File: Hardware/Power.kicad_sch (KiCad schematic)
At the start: 0 parts

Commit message: RP3254B power connections
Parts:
- added L2: L_Small, symbol Device:L_Small
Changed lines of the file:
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@@
 		(company "J. Thweatt")
 	)
+	(symbol
+		(lib_id "Device:L_Small")
+		(at 179.07 127 0)
+		(unit 1)
+		(body_style 1)
+		(exclude_from_sim no)
+		(in_bom yes)
+		(on_board yes)
+		(in_pos_files yes)
+		(dnp no)
+		(fields_autoplaced yes)
+		(property "Reference" "L2"
+			(at 180.34 125.7299 0)
+			(show_name no)
+			(do_not_autoplace no)
+			(effects
+				(font
+					(size 1.27 1.27)
+				)
+				(justify left)
+			)
+		)
+		(property "Value" "L_Small"
+			(at 180.34 128.2699 0)
+			(show_name no)
+			(do_not_autoplace no)
+			(effects
+				(font
+					(size 1.27 1.27)
+				)
+				(justify left)
+			)
+		)
+		(property "Footprint" ""
+			(at 179.07 127 0)
+			(hide yes)
+			(show_name no)
+			(do_not_autoplace no)
+			(effects
+				(font
+					(size 1.27 1.27)
+				)
+			)
+		)
+		(property "Datasheet" ""
+			(at 179.07 127 0)
+			(hide yes)
+			(show_name no)
+			(do_not_autoplace no)
+			(effects
+				(font
+					(size 1.27 1.27)
+				)
+			)
+		)
+		(property "Description" "Inductor, small symbol"
+			(at 179.07 127 0)
+			(hide yes)
+			(show_name no)
+			(do_not_autoplace no)
+			(effects
+				(font
+					(size 1.27 1.27)
+				)
+			)
+		)
+		(pin "2"
+		)
+		(pin "1"
+		)
+		(instances
+			(project "digichiver"
+				(path "/51de4045-d2a2-42d9-b145-319acd726bb6/3f31dd03-db19-4d71-92cd-90eb39c94774"
+					(reference "L2")
+					(unit 1)
+				)
+			)
+		)
+	)
 )

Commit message: sync
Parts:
- added C31: 10uF, symbol Device:C
- added C32: 22uF, symbol Device:C
- added J2: USB_C_Receptacle, symbol Connector:USB_C_Receptacle
- added L3: 1uH, symbol Device:L_Small
- added R14: 1k, symbol Device:R_US
- added U7: TLV61046A, symbol Digichiver:TLV61046A
- added U8: TPS62903, symbol Digichiver:TPS62903
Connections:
- new net: J2.A1 (GND), J2.A12 (GND), J2.B1 (GND), J2.B12 (GND)
- new net: J2.A4 (VBUS), J2.A9 (VBUS), J2.B4 (VBUS), J2.B9 (VBUS)
- new net: L3.1, U8.2 (SW)
- no-connect marks 0 -> 2
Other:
- moved on the sheet: L2

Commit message: power
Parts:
- removed J2: USB_C_Receptacle, symbol Connector:USB_C_Receptacle
- removed L3: 1uH, symbol Device:L_Small
- added C33: 1uF, symbol Device:C
- added C34: 4.7uF, symbol Device:C
- added C35: 22uF, symbol Device:C
- added J3, J4: 61300211121, symbol Connector:Conn_01x02_Pin
- added R15: 18K, symbol Device:R_US
- added R16: 71.5k, symbol Device:R_US
- added R17: 45.3K, symbol Device:R_US
- added R18: 10K, symbol Device:R_US
- L2: value L_Small -> 15uH
- R14: value 1k -> 732k
- U8: value TPS62903 -> TPSM84338
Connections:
- net +5V: now reaches L2.1
- net +5V: now also C31.1, U7.4 (EN), U7.6 (VIN), U8.1 (EN), U8.6 (VIN), C33.1
- net at L2.2: now also U7.1 (SW)
- net +9V_RAW: now reaches R14.1
- net +9V_RAW: now also U7.5 (VOUT), C34.1, J4.1 (Pin_1)
- net at R14.2: now also U7.3 (FB), R16.1
- net GND: now reaches U7.2 (GND)
- net GND: now also C31.2, C32.2, U8.3 (GND), U8.9 (RT/SYNC), C33.2, C34.2, C35.2, R15.2, R16.2, R18.2
- net +3V3_RAW: now reaches C32.1
- net +3V3_RAW: now also U8.4 (VOUT), C35.1, J3.1 (Pin_1), R17.1
- net at U8.2 (FB): now also R17.2, R18.1
- net at U8.7 (MODE): now also R15.1
- new net +3.3V: J3.2 (Pin_2)
- new net +9V: J4.2 (Pin_2)
- no-connect marks 2 -> 1
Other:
- moved on the sheet: C31, C32, L2, R14, U7

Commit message: footprint assignment
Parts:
- C31: footprint (none) -> Capacitor_SMD:C_0402_1005Metric; MPN (none) -> CL05A106MQ5NUNC
- C32, C35: footprint (none) -> Capacitor_SMD:C_0603_1608Metric; MPN (none) -> CL10A226MQ8NRNC
- C33: footprint (none) -> Capacitor_SMD:C_0402_1005Metric; MPN (none) -> CL05A105KA5NQNC
- C34: footprint (none) -> Capacitor_SMD:C_0603_1608Metric; MPN (none) -> CL10A475KA8NQNC
- J3, J4: footprint (none) -> Connector_PinHeader_1.00mm:PinHeader_1x02_P1.00mm_Vertical; MPN (none) -> 61300211121
- L2: MPN (none) -> VLCF4020T-150MR68
- U7: footprint (none) -> Package_TO_SOT_SMD:SOT-23-6; MPN (none) -> TLV61046A
- U8: MPN (none) -> TPSM84338

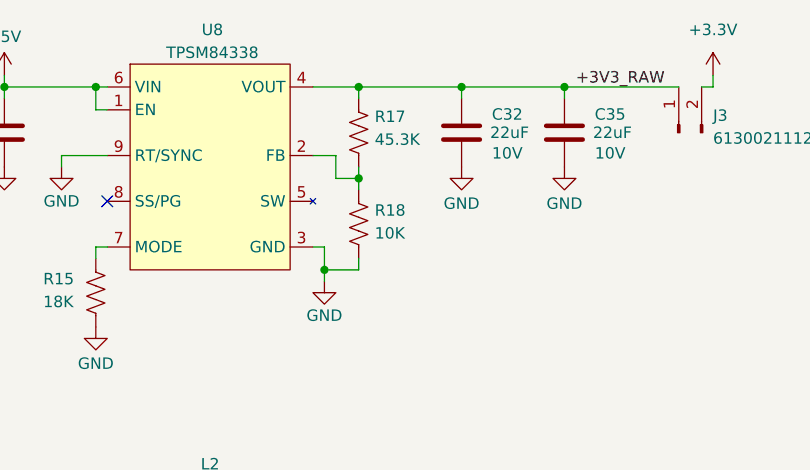
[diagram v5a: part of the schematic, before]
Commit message: link footprints to symbols
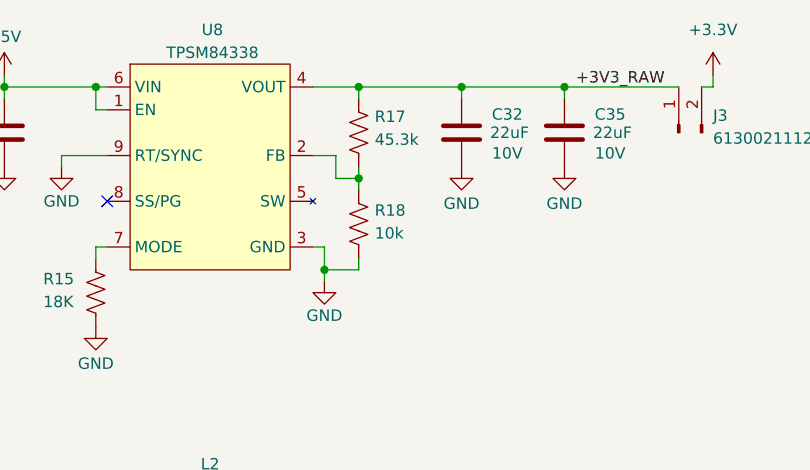
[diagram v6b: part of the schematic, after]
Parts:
- L2: footprint (none) -> Digichiver:IND_VLCF4020T-150MR68
- R14: footprint (none) -> Resistor_SMD:R_0402_1005Metric; MPN (none) -> RC0402FR-07732KL
- R15: footprint (none) -> Resistor_SMD:R_0402_1005Metric; MPN (none) -> RC0402FR-0718KL
- R16: footprint (none) -> Resistor_SMD:R_0402_1005Metric; MPN (none) -> RC0402FR-0771K5L
- R17: value 45.3K -> 45.3k; footprint (none) -> Resistor_SMD:R_0402_1005Metric; MPN (none) -> RC0402FR-0745K3L
- R18: value 10K -> 10k; footprint (none) -> Resistor_SMD:R_0402_1005Metric; MPN (none) -> RC0402FR-0710KL
- U8: footprint (none) -> Digichiver:CONV_TPSM84338RCJR
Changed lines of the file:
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@@
 			)
 		)
-		(property "Footprint" ""
+		(property "Footprint" "Digichiver:IND_VLCF4020T-150MR68"
 			(at 209.55 144.78 0)
 			(hide yes)
@@
 			)
 		)
-		(property "Footprint" ""
+		(property "Footprint" "Digichiver:CONV_TPSM84338RCJR"
 			(at 213.36 92.71 0)
 			(hide yes)
@@
 			)
 		)
-		(property "Value" "10K"
+		(property "Value" "10k"
 			(at 227.838 114.046 0)
 			(show_name no)
@@
 			)
 		)
-		(property "Footprint" ""
+		(property "Footprint" "Resistor_SMD:R_0402_1005Metric"
 			(at 227.076 113.284 90)
 			(hide yes)
@@
 			)
 		)
-		(property "Datasheet" ""
+		(property "Datasheet" "https://yageogroup.com/content/datasheet/asset/file/PYU-RC_GROUP_51_ROHS_L"
 			(at 226.06 113.03 0)
 			(hide yes)
@@
 		)
 		(property "KLC_S4.2_VREG_LX" ""
+			(at 226.06 113.03 0)
+			(hide yes)
+			(show_name no)
+			(do_not_autoplace no)
+			(effects
+				(font
+					(size 1.27 1.27)
+				)
+			)
+		)
+		(property "MPN" "RC0402FR-0710KL"
 			(at 226.06 113.03 0)
 			(hide yes)
@@
 			)
 		)
-		(property "Footprint" ""
+		(property "Footprint" "Resistor_SMD:R_0402_1005Metric"
 			(at 224.536 164.084 90)
 			(hide yes)
@@
 			)
 		)
-		(property "Datasheet" ""
+		(property "Datasheet" "https://yageogroup.com/content/datasheet/asset/file/PYU-RC_GROUP_51_ROHS_L"
 			(at 223.52 163.83 0)
 			(hide yes)
@@
 		)
 		(property "KLC_S4.2_VREG_LX" ""
+			(at 223.52 163.83 0)
+			(hide yes)
+			(show_name no)
+			(do_not_autoplace no)
+			(effects
+				(font
+					(size 1.27 1.27)
+				)
+			)
+		)
+		(property "MPN" "RC0402FR-07732KL"
 			(at 223.52 163.83 0)
 			(hide yes)
@@
 			)
 		)
-		(property "Footprint" ""
+		(property "Footprint" "Resistor_SMD:R_0402_1005Metric"
 			(at 224.536 174.244 90)
 			(hide yes)
@@
 			)
 		)
-		(property "Datasheet" ""
+		(property "Datasheet" "https://yageogroup.com/content/datasheet/asset/file/PYU-RC_GROUP_51_ROHS_L"
 			(at 223.52 173.99 0)
 			(hide yes)
@@
 		)
 		(property "KLC_S4.2_VREG_LX" ""
+			(at 223.52 173.99 0)
+			(hide yes)
+			(show_name no)
+			(do_not_autoplace no)
+			(effects
+				(font
+					(size 1.27 1.27)
+				)
+			)
+		)
+		(property "MPN" "RC0402FR-0771K5L"
 			(at 223.52 173.99 0)
 			(hide yes)
@@
 			)
 		)
-		(property "Value" "45.3K"
+		(property "Value" "45.3k"
 			(at 227.838 103.632 0)
 			(show_name no)
@@
 			)
 		)
-		(property "Footprint" ""
+		(property "Footprint" "Resistor_SMD:R_0402_1005Metric"
 			(at 227.076 103.124 90)
 			(hide yes)
@@
 			)
 		)
-		(property "Datasheet" ""
+		(property "Datasheet" "https://yageogroup.com/content/datasheet/asset/file/PYU-RC_GROUP_51_ROHS_L"
 			(at 226.06 102.87 0)
 			(hide yes)
@@
 		)
 		(property "KLC_S4.2_VREG_LX" ""
+			(at 226.06 102.87 0)
+			(hide yes)
+			(show_name no)
+			(do_not_autoplace no)
+			(effects
+				(font
+					(size 1.27 1.27)
+				)
+			)
+		)
+		(property "MPN" "RC0402FR-0745K3L"
 			(at 226.06 102.87 0)
 			(hide yes)
@@
 			)
 		)
-		(property "Footprint" ""
+		(property "Footprint" "Resistor_SMD:R_0402_1005Metric"
 			(at 197.866 120.904 90)
 			(hide yes)
@@
 			)
 		)
-		(property "Datasheet" ""
+		(property "Datasheet" "https://yageogroup.com/content/datasheet/asset/file/PYU-RC_GROUP_51_ROHS_L"
 			(at 196.85 120.65 0)
 			(hide yes)
@@
 			(at 196.85 120.65 0)
 			(hide yes)
+			(show_name no)
+			(do_not_autoplace no)
+			(effects
+				(font
+					(size 1.27 1.27)
+				)
+			)
+		)
+		(property "MPN" "RC0402FR-0718KL"
+			(at 196.85 120.65 0)
+			(hide yes)

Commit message: generate outputs
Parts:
- C31: JLCPCB Part # (none) -> C315248; MPN CL05A106MQ5NUNC -> CL05A106MP5NUNC
- C32, C35: JLCPCB Part # (none) -> C59461
- C33: JLCPCB Part # (none) -> C52923; Voltage 10V -> 25V
- C34: footprint Capacitor_SMD:C_0603_1608Metric -> Capacitor_SMD:C_0402_1005Metric; JLCPCB Part # (none) -> C318563; MPN CL10A475KA8NQNC -> CL05A475MO5NUNC
- J3, J4: JLCPCB Part # (none) -> C2915055
- L2: JLCPCB Part # (none) -> C695173
- R14: JLCPCB Part # (none) -> C137940
- R15: JLCPCB Part # (none) -> C138044
- R16: JLCPCB Part # (none) -> C273328
- R17: JLCPCB Part # (none) -> C137977
- R18: JLCPCB Part # (none) -> C60490
- U7: JLCPCB Part # (none) -> C139398
- U8: JLCPCB Part # (none) -> C47122151
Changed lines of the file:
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@@
 			)
 		)
-		(property "Footprint" "Capacitor_SMD:C_0603_1608Metric"
+		(property "Footprint" "Capacitor_SMD:C_0402_1005Metric"
 			(at 234.6452 167.64 0)
 			(hide yes)
@@
 			)
 		)
-		(property "MPN" "CL10A475KA8NQNC"
+		(property "MPN" "CL05A475MO5NUNC"
 			(at 233.68 163.83 0)
 			(hide yes)
@@
 		)
 		(property "KLC_S4.2_VREG_LX" ""
+			(at 233.68 163.83 0)
+			(hide yes)
+			(show_name no)
+			(do_not_autoplace no)
+			(effects
+				(font
+					(size 1.27 1.27)
+				)
+			)
+		)
+		(property "JLCPCB Part #" "C318563"
 			(at 233.68 163.83 0)
 			(hide yes)
@@
 			)
 		)
+		(property "JLCPCB Part #" "C695173"
+			(at 209.55 144.78 90)
+			(hide yes)
+			(show_name no)
+			(do_not_autoplace no)
+			(effects
+				(font
+					(size 1.27 1.27)
+				)
+			)
+		)
 		(pin "2"
 		)
@@
 			)
 		)
+		(property "JLCPCB Part #" "C47122151"
+			(at 213.36 92.71 0)
+			(hide yes)
+			(show_name no)
+			(do_not_autoplace no)
+			(effects
+				(font
+					(size 1.27 1.27)
+				)
+			)
+		)
 		(pin "6"
 		)
@@
 			)
 		)
+		(property "JLCPCB Part #" "C60490"
+			(at 226.06 113.03 0)
+			(hide yes)
+			(show_name no)
+			(do_not_autoplace no)
+			(effects
+				(font
+					(size 1.27 1.27)
+				)
+			)
+		)
 		(pin "1"
 		)
@@
 		)
 		(property "MPN" "RC0402FR-07732KL"
+			(at 223.52 163.83 0)
+			(hide yes)
+			(show_name no)
+			(do_not_autoplace no)
+			(effects
+				(font
+					(size 1.27 1.27)
+				)
+			)
+		)
+		(property "JLCPCB Part #" "C137940"
 			(at 223.52 163.83 0)
 			(hide yes)
@@
 			)
 		)
+		(property "JLCPCB Part #" "C2915055"
+			(at 247.65 163.83 90)
+			(hide yes)
+			(show_name no)
+			(do_not_autoplace no)
+			(effects
+				(font
+					(size 1.27 1.27)
+				)
+			)
+		)
 		(pin "1"
 		)
@@
 			)
 		)
+		(property "JLCPCB Part #" "C59461"
+			(at 248.92 102.87 0)
+			(hide yes)
+			(show_name no)
+			(do_not_autoplace no)
+			(effects
+				(font
+					(size 1.27 1.27)
+				)
+			)
+		)
 		(pin "2"
 		)
@@
 			)
 		)
+		(property "JLCPCB Part #" "C139398"
+			(at 213.36 148.59 0)
+			(hide yes)
+			(show_name no)
+			(do_not_autoplace no)
+			(effects
+				(font
+					(size 1.27 1.27)
+				)
+			)
+		)
 		(pin "6"
 		)
@@
 			)
 		)
-		(property "Voltage" "10V"
+		(property "Voltage" "25V"
 			(at 186.182 161.036 0)
 			(show_name no)
@@
 		)
 		(property "KLC_S4.2_VREG_LX" ""
+			(at 191.77 158.75 0)
+			(hide yes)
+			(show_name no)
+			(do_not_autoplace no)
+			(effects
+				(font
+					(size 1.27 1.27)
+				)
+			)
+		)
+		(property "JLCPCB Part #" "C52923"
 			(at 191.77 158.75 0)
 			(hide yes)
@@
 			)
 		)
+		(property "JLCPCB Part #" "C59461"
+			(at 237.49 102.87 0)
+			(hide yes)
+			(show_name no)
+			(do_not_autoplace no)
+			(effects
+				(font
+					(size 1.27 1.27)
+				)
+			)
+		)
 		(pin "2"
 		)
@@
 			)
 		)
+		(property "JLCPCB Part #" "C273328"
+			(at 223.52 173.99 0)
+			(hide yes)
+			(show_name no)
+			(do_not_autoplace no)
+			(effects
+				(font
+					(size 1.27 1.27)
+				)
+			)
+		)
 		(pin "1"
 		)
@@
 			)
 		)
+		(property "JLCPCB Part #" "C137977"
+			(at 226.06 102.87 0)
+			(hide yes)
+			(show_name no)
+			(do_not_autoplace no)
+			(effects
+				(font
+					(size 1.27 1.27)
+				)
+			)
+		)
 		(pin "1"
 		)
@@
 			)
 		)
+		(property "JLCPCB Part #" "C138044"
+			(at 196.85 120.65 0)
+			(hide yes)
+			(show_name no)
+			(do_not_autoplace no)
+			(effects
+				(font
+					(size 1.27 1.27)
+				)
+			)
+		)
 		(pin "1"
 		)
@@
 			)
 		)
-		(property "MPN" "CL05A106MQ5NUNC"
+		(property "MPN" "CL05A106MP5NUNC"
 			(at 186.69 102.87 0)
 			(hide yes)
@@
 		)
 		(property "KLC_S4.2_VREG_LX" ""
+			(at 186.69 102.87 0)
+			(hide yes)
+			(show_name no)
+			(do_not_autoplace no)
+			(effects
+				(font
+					(size 1.27 1.27)
+				)
+			)
+		)
+		(property "JLCPCB Part #" "C315248"
 			(at 186.69 102.87 0)
 			(hide yes)
@@
 			(at 261.62 102.87 90)
 			(hide yes)
+			(show_name no)
+			(do_not_autoplace no)
+			(effects
+				(font
+					(size 1.27 1.27)
+				)
+			)
+		)
+		(property "JLCPCB Part #" "C2915055"
+			(at 261.62 102.87 90)
+			(hide yes)
